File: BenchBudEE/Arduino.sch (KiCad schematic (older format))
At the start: 0 parts

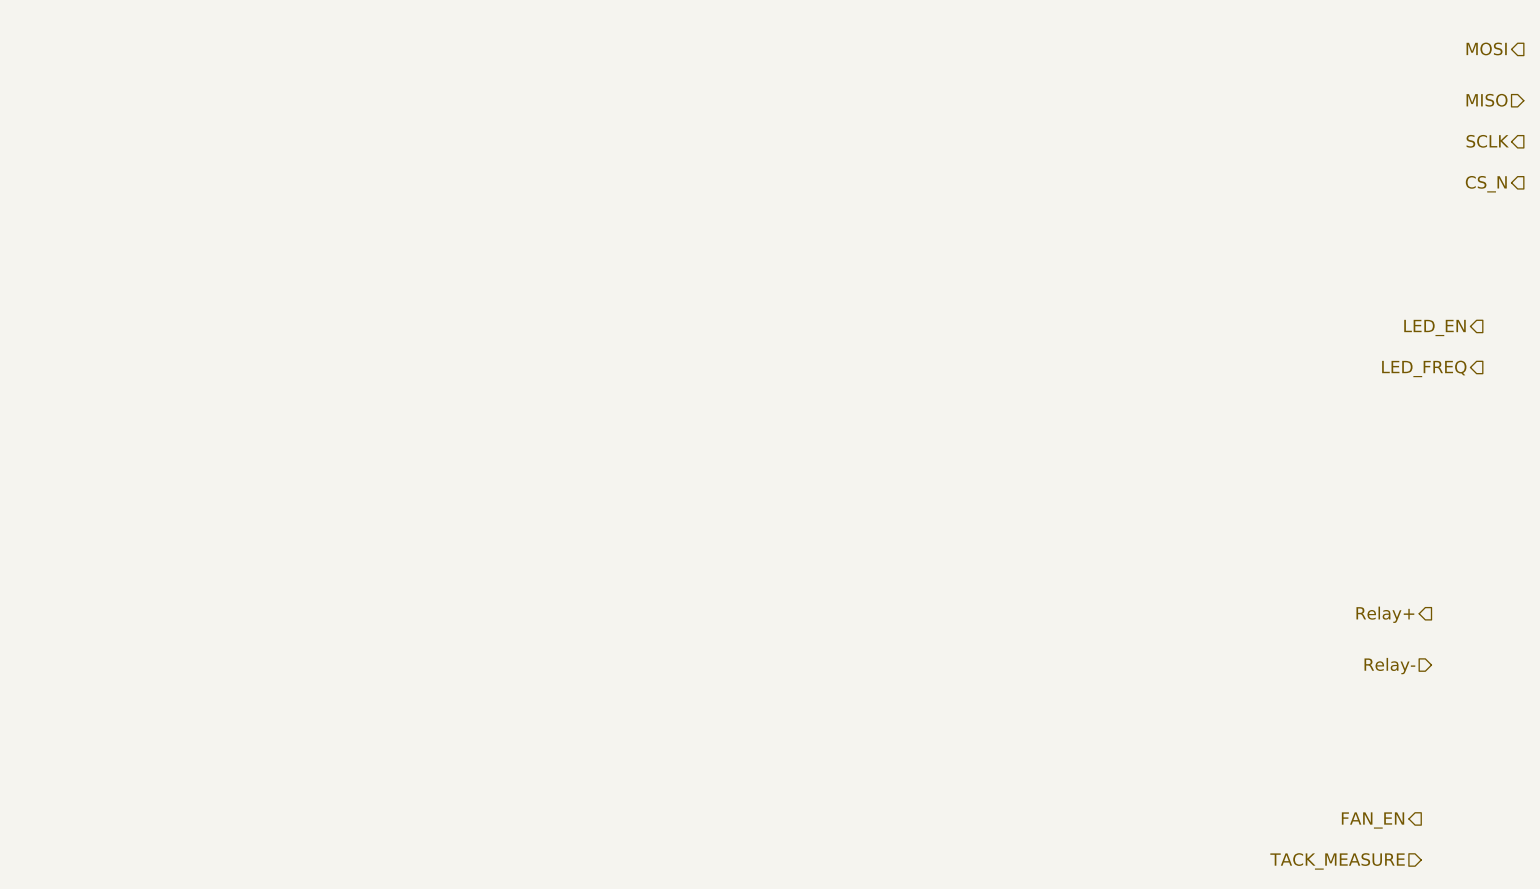
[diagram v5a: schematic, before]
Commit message: Schematic modules connected together and to arduino pins
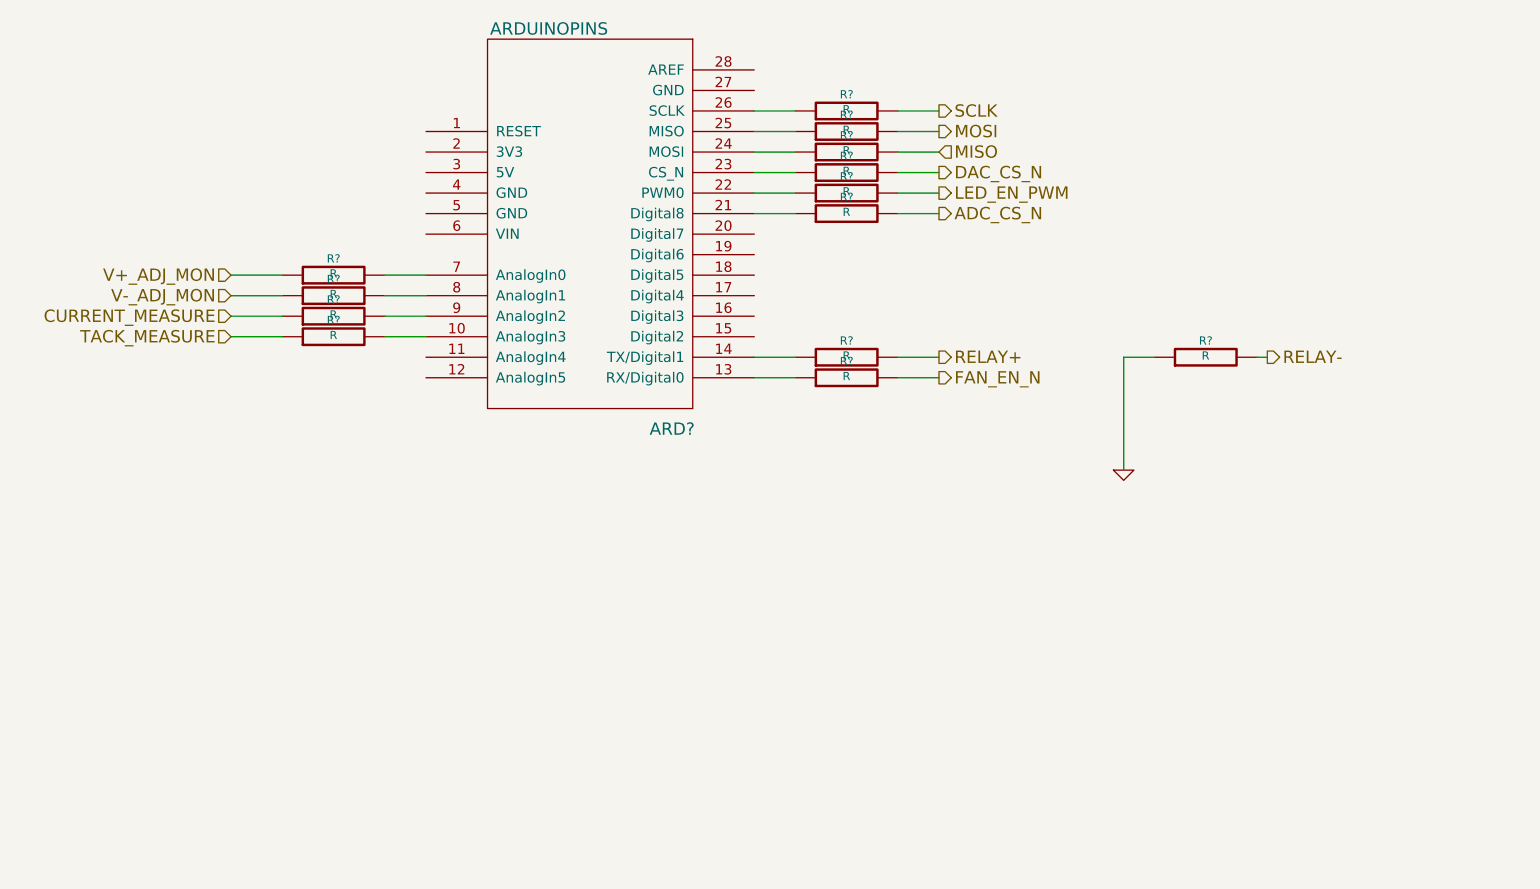
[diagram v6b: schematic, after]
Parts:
- added ARD?: ARDUINOPINS, symbol ARDUINOPINS
- added R? (x13): R, ~, symbol R
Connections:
- net MISO: now also R?.2
- net MOSI: now also R?.2
- net SCLK: now also R?.2
- net TACK_MEASURE: now also R?.1
- new net: ARD?.10 (AnalogIn3), R?.2
- new net: ARD?.13 (RX/Digital0), R?.1
- new net: ARD?.14 (TX/Digital1), R?.1
- new net: ARD?.21 (Digital8), R?.1
- new net: ARD?.22 (PWM0), R?.1
- new net: ARD?.23 (CS_N), R?.1
- new net: ARD?.24 (MOSI), R?.1
- new net: ARD?.25 (MISO), R?.1
- new net: ARD?.26 (SCLK), R?.1
- new net: ARD?.7 (AnalogIn0), R?.2
- new net: ARD?.8 (AnalogIn1), R?.2
- new net: ARD?.9 (AnalogIn2), R?.2
- new net ADC_CS_N: R?.2
- new net CURRENT_MEASURE: R?.1
- new net DAC_CS_N: R?.2
- new net FAN_EN_N: R?.2
- new net GND: R?.1
- new net LED_EN_PWM: R?.2
- new net RELAY+: R?.2
- new net RELAY-: R?.2
- new net V+_ADJ_MON: R?.1
- new net V-_ADJ_MON: R?.1

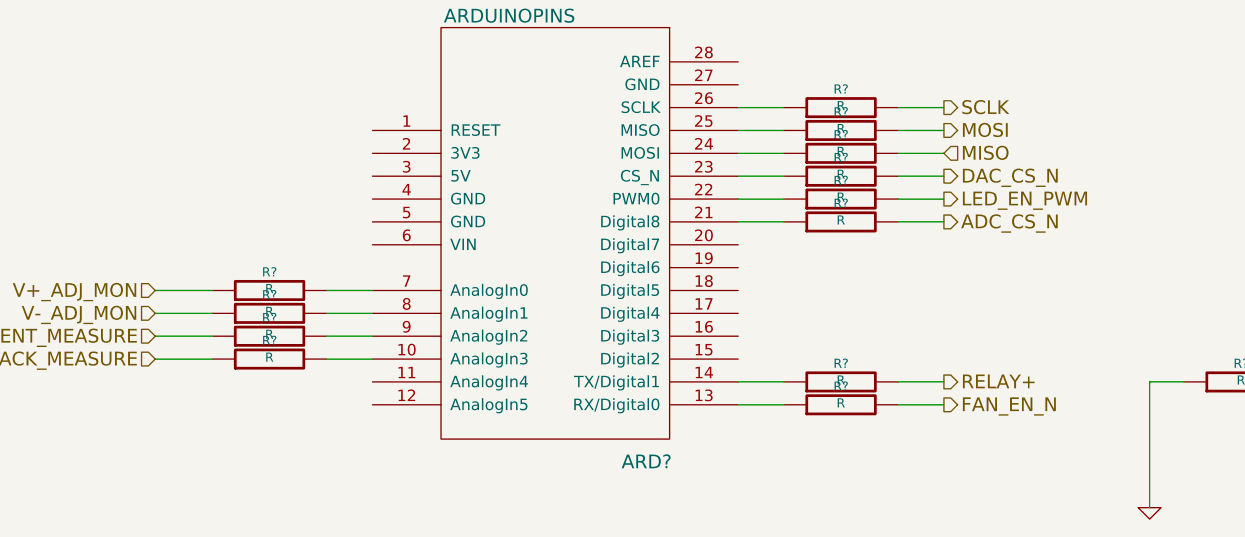
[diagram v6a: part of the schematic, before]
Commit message: Parts added to relay module. Schematic tidied up.
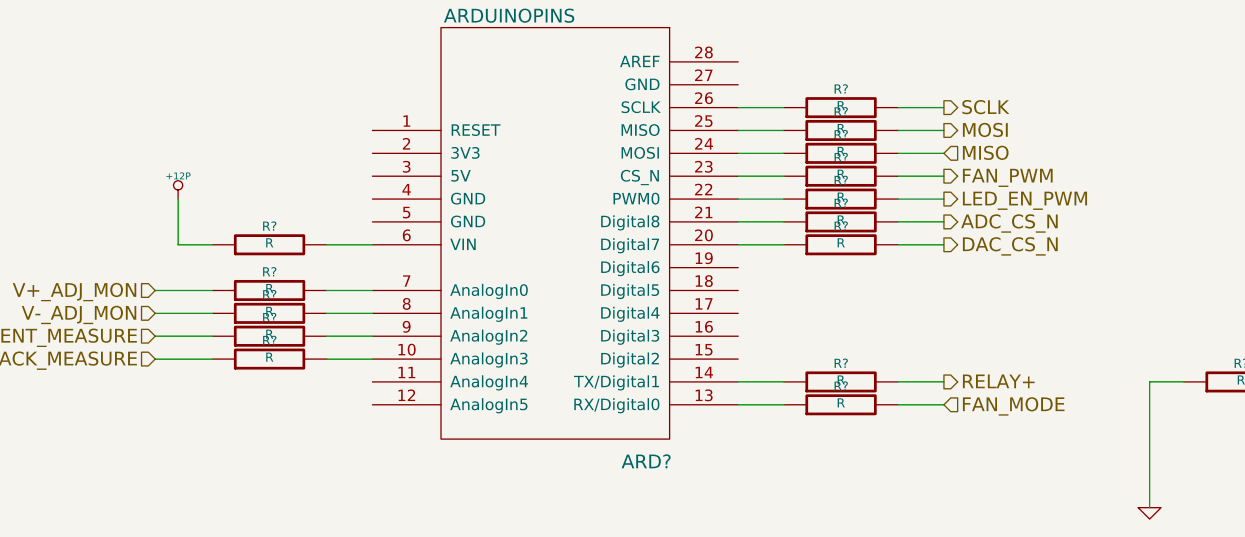
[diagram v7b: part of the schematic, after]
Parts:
- removed R?: R, ~, symbol R
- added R? (x3): R, ~, symbol R
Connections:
- net DAC_CS_N: now also R?.2; no longer R?.2
- net at ARD?.13 (RX/Digital0): now also R?.1
- net at ARD?.20 (Digital7): now also R?.1
- net at ARD?.6 (VIN): now also R?.2
- new net +12P: R?.1
- new net FAN_MODE: R?.2
- new net FAN_PWM: R?.2
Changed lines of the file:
@@
 Sheet 9 9
 Title ""
-Date "8 feb 2014"
+Date "19 feb 2014"
 Rev ""
 Comp ""
@@
 Text HLabel 7700 1800 2    60   Output ~ 0
 SCLK
-Text HLabel 7700 2100 2    60   Output ~ 0
+Text HLabel 7700 2400 2    60   Output ~ 0
 DAC_CS_N
 Text HLabel 7700 3000 2    60   Output ~ 0
@@
 Text HLabel 7700 2200 2    60   Output ~ 0
 LED_EN_PWM
-Text HLabel 7700 3100 2    60   Output ~ 0
-FAN_EN_N
+Text HLabel 7700 2100 2    60   Output ~ 0
+FAN_PWM
 Text HLabel 4250 2900 0    60   Input ~ 0
 TACK_MEASURE
@@
 $Comp
 L R R?
-U 1 1 52F67364
-P 7250 3100
-F 0 "R?" V 7330 3100 40  0000 C CNN
-F 1 "R" V 7257 3101 40  0000 C CNN
-F 2 "~" V 7180 3100 30  0000 C CNN
-F 3 "~" H 7250 3100 30  0000 C CNN
-	1    7250 3100
-	0    -1   -1   0
-$EndComp
-Wire Wire Line
-	6800 3100 7000 3100
-Wire Wire Line
-	7500 3100 7700 3100
-$Comp
-L R R?
 U 1 1 52F67CB3
 P 7250 3000
@@
 Wire Wire Line
 	7500 2300 7700 2300
+$Comp
+L R R?
+U 1 1 52F82098
+P 7250 2400
+F 0 "R?" V 7330 2400 40  0000 C CNN
+F 1 "R" V 7257 2401 40  0000 C CNN
+F 2 "~" V 7180 2400 30  0000 C CNN
+F 3 "~" H 7250 2400 30  0000 C CNN
+	1    7250 2400
+	0    -1   -1   0
+$EndComp
+Wire Wire Line
+	7500 2400 7700 2400
+Wire Wire Line
+	7000 2400 6800 2400
+Text HLabel 7700 3100 2    60   Input ~ 0
+FAN_MODE
+$Comp
+L R R?
+U 1 1 52F826E8
+P 7250 3100
+F 0 "R?" V 7330 3100 40  0000 C CNN
+F 1 "R" V 7257 3101 40  0000 C CNN
+F 2 "~" V 7180 3100 30  0000 C CNN
+F 3 "~" H 7250 3100 30  0000 C CNN
+	1    7250 3100
+	0    -1   -1   0
+$EndComp
+Wire Wire Line
+	7500 3100 7700 3100
+Wire Wire Line
+	7000 3100 6800 3100
+$Comp
+L R R?
+U 1 1 52F82727
+P 4750 2400
+F 0 "R?" V 4830 2400 40  0000 C CNN
+F 1 "R" V 4757 2401 40  0000 C CNN
+F 2 "~" V 4680 2400 30  0000 C CNN
+F 3 "~" H 4750 2400 30  0000 C CNN
+	1    4750 2400
+	0    -1   -1   0
+$EndComp
+Wire Wire Line
+	5000 2400 5200 2400
+$Comp
+L +12P #PWR?
+U 1 1 52F8274D
+P 4350 2200
+F 0 "#PWR?" H 4350 2170 30  0001 C CNN
+F 1 "+12P" H 4350 2300 30  0000 C CNN
+F 2 "" H 4350 2200 60  0000 C CNN
+F 3 "" H 4350 2200 60  0000 C CNN
+	1    4350 2200
+	1    0    0    -1
+$EndComp
+Wire Wire Line
+	4350 2200 4350 2400
+Wire Wire Line
+	4350 2400 4500 2400
 $EndSCHEMATC

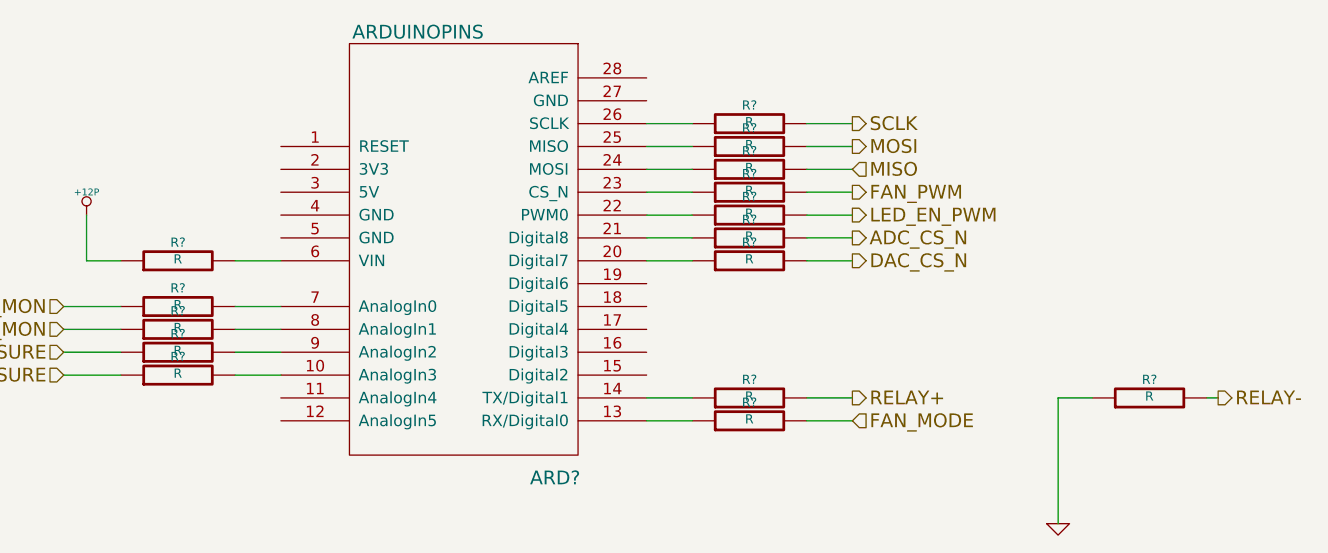
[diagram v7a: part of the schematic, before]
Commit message: Design rules specified for layout.
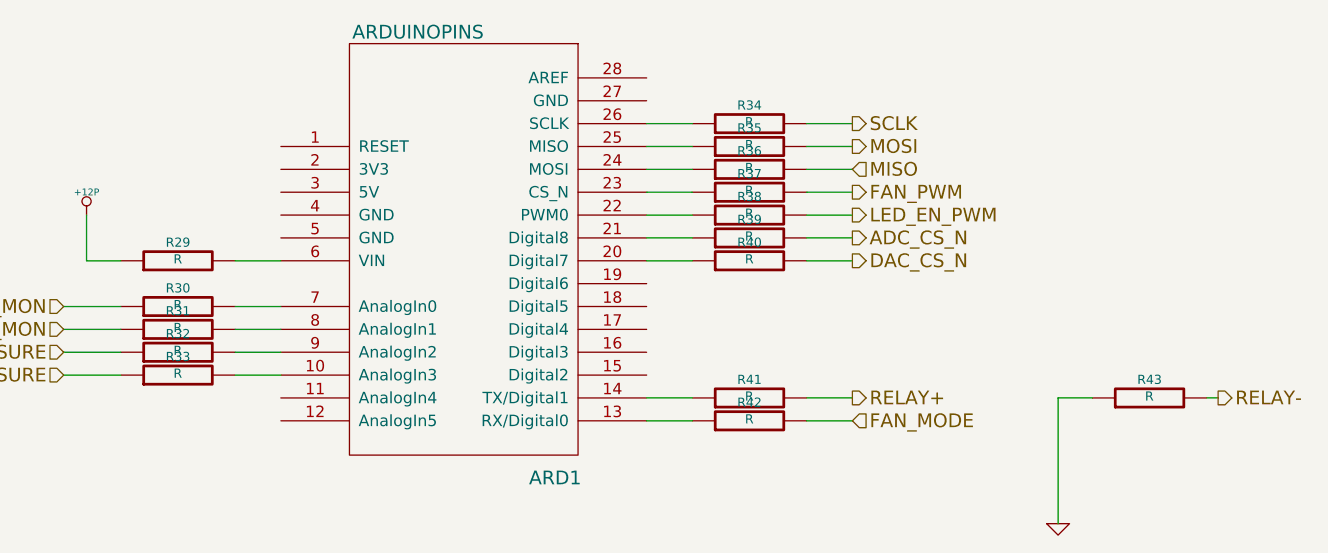
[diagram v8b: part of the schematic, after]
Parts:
- gave numbers to parts that had none: 16
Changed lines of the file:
@@
 TACK_MEASURE
 $Comp
-L ARDUINOPINS ARD?
+L ARDUINOPINS ARD1
 U 1 1 52F62ADF
 P 6250 2150
-F 0 "ARD?" H 6400 950 60  0000 C CNN
+F 0 "ARD1" H 6400 950 60  0000 C CNN
 F 1 "ARDUINOPINS" H 5800 2900 60  0000 C CNN
 F 2 "" H 6250 2150 60  0000 C CNN
@@
 CURRENT_MEASURE
 $Comp
-L R R?
+L R R41
 U 1 1 52F67CB3
 P 7250 3000
-F 0 "R?" V 7330 3000 40  0000 C CNN
+F 0 "R41" V 7330 3000 40  0000 C CNN
 F 1 "R" V 7257 3001 40  0000 C CNN
 F 2 "~" V 7180 3000 30  0000 C CNN
@@
 	7000 3000 6800 3000
 $Comp
-L GND #PWR?
+L GND #PWR55
 U 1 1 52F67CCE
 P 8600 3550
-F 0 "#PWR?" H 8600 3550 30  0001 C CNN
+F 0 "#PWR55" H 8600 3550 30  0001 C CNN
 F 1 "GND" H 8600 3480 30  0001 C CNN
 F 2 "" H 8600 3550 60  0000 C CNN
@@
 	8600 3000 8600 3550
 $Comp
-L R R?
+L R R33
 U 1 1 52F67CEA
 P 4750 2900
-F 0 "R?" V 4830 2900 40  0000 C CNN
+F 0 "R33" V 4830 2900 40  0000 C CNN
 F 1 "R" V 4757 2901 40  0000 C CNN
 F 2 "~" V 4680 2900 30  0000 C CNN
@@
 	4500 2900 4250 2900
 $Comp
-L R R?
+L R R32
 U 1 1 52F67D10
 P 4750 2800
-F 0 "R?" V 4830 2800 40  0000 C CNN
+F 0 "R32" V 4830 2800 40  0000 C CNN
 F 1 "R" V 4757 2801 40  0000 C CNN
 F 2 "~" V 4680 2800 30  0000 C CNN
@@
 V-_ADJ_MON
 $Comp
-L R R?
+L R R31
 U 1 1 52F6880D
 P 4750 2700
-F 0 "R?" V 4830 2700 40  0000 C CNN
+F 0 "R31" V 4830 2700 40  0000 C CNN
 F 1 "R" V 4757 2701 40  0000 C CNN
 F 2 "~" V 4680 2700 30  0000 C CNN
@@
 $EndComp
 $Comp
-L R R?
+L R R30
 U 1 1 52F68813
 P 4750 2600
-F 0 "R?" V 4830 2600 40  0000 C CNN
+F 0 "R30" V 4830 2600 40  0000 C CNN
 F 1 "R" V 4757 2601 40  0000 C CNN
 F 2 "~" V 4680 2600 30  0000 C CNN
@@
 	5000 2700 5200 2700
 $Comp
-L R R?
+L R R37
 U 1 1 52F6885D
 P 7250 2100
-F 0 "R?" V 7330 2100 40  0000 C CNN
+F 0 "R37" V 7330 2100 40  0000 C CNN
 F 1 "R" V 7257 2101 40  0000 C CNN
 F 2 "~" V 7180 2100 30  0000 C CNN
@@
 $EndComp
 $Comp
-L R R?
+L R R36
 U 1 1 52F6886D
 P 7250 2000
-F 0 "R?" V 7330 2000 40  0000 C CNN
+F 0 "R36" V 7330 2000 40  0000 C CNN
 F 1 "R" V 7257 2001 40  0000 C CNN
 F 2 "~" V 7180 2000 30  0000 C CNN
@@
 $EndComp
 $Comp
-L R R?
+L R R35
 U 1 1 52F68873
 P 7250 1900
-F 0 "R?" V 7330 1900 40  0000 C CNN
+F 0 "R35" V 7330 1900 40  0000 C CNN
 F 1 "R" V 7257 1901 40  0000 C CNN
 F 2 "~" V 7180 1900 30  0000 C CNN
@@
 $EndComp
 $Comp
-L R R?
+L R R34
 U 1 1 52F68879
 P 7250 1800
-F 0 "R?" V 7330 1800 40  0000 C CNN
+F 0 "R34" V 7330 1800 40  0000 C CNN
 F 1 "R" V 7257 1801 40  0000 C CNN
 F 2 "~" V 7180 1800 30  0000 C CNN
@@
 	7000 1800 6800 1800
 $Comp
-L R R?
+L R R43
 U 1 1 52F68915
 P 9000 3000
-F 0 "R?" V 9080 3000 40  0000 C CNN
+F 0 "R43" V 9080 3000 40  0000 C CNN
 F 1 "R" V 9007 3001 40  0000 C CNN
 F 2 "~" V 8930 3000 30  0000 C CNN
@@
 	8750 3000 8600 3000
 $Comp
-L R R?
+L R R38
 U 1 1 52F6894B
 P 7250 2200
-F 0 "R?" V 7330 2200 40  0000 C CNN
+F 0 "R38" V 7330 2200 40  0000 C CNN
 F 1 "R" V 7257 2201 40  0000 C CNN
 F 2 "~" V 7180 2200 30  0000 C CNN
@@
 	7000 2200 6800 2200
 $Comp
-L R R?
+L R R39
 U 1 1 52F6DE61
 P 7250 2300
-F 0 "R?" V 7330 2300 40  0000 C CNN
+F 0 "R39" V 7330 2300 40  0000 C CNN
 F 1 "R" V 7257 2301 40  0000 C CNN
 F 2 "~" V 7180 2300 30  0000 C CNN
@@
 	7500 2300 7700 2300
 $Comp
-L R R?
+L R R40
 U 1 1 52F82098
 P 7250 2400
-F 0 "R?" V 7330 2400 40  0000 C CNN
+F 0 "R40" V 7330 2400 40  0000 C CNN
 F 1 "R" V 7257 2401 40  0000 C CNN
 F 2 "~" V 7180 2400 30  0000 C CNN
@@
 FAN_MODE
 $Comp
-L R R?
+L R R42
 U 1 1 52F826E8
 P 7250 3100
-F 0 "R?" V 7330 3100 40  0000 C CNN
+F 0 "R42" V 7330 3100 40  0000 C CNN
 F 1 "R" V 7257 3101 40  0000 C CNN
 F 2 "~" V 7180 3100 30  0000 C CNN
@@
 	7000 3100 6800 3100
 $Comp
-L R R?
+L R R29
 U 1 1 52F82727
 P 4750 2400
-F 0 "R?" V 4830 2400 40  0000 C CNN
+F 0 "R29" V 4830 2400 40  0000 C CNN
 F 1 "R" V 4757 2401 40  0000 C CNN
 F 2 "~" V 4680 2400 30  0000 C CNN
@@
 	5000 2400 5200 2400
 $Comp
-L +12P #PWR?
+L +12P #PWR54
 U 1 1 52F8274D
 P 4350 2200
-F 0 "#PWR?" H 4350 2170 30  0001 C CNN
+F 0 "#PWR54" H 4350 2170 30  0001 C CNN
 F 1 "+12P" H 4350 2300 30  0000 C CNN
 F 2 "" H 4350 2200 60  0000 C CNN
